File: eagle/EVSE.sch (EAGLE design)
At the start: 21 parts

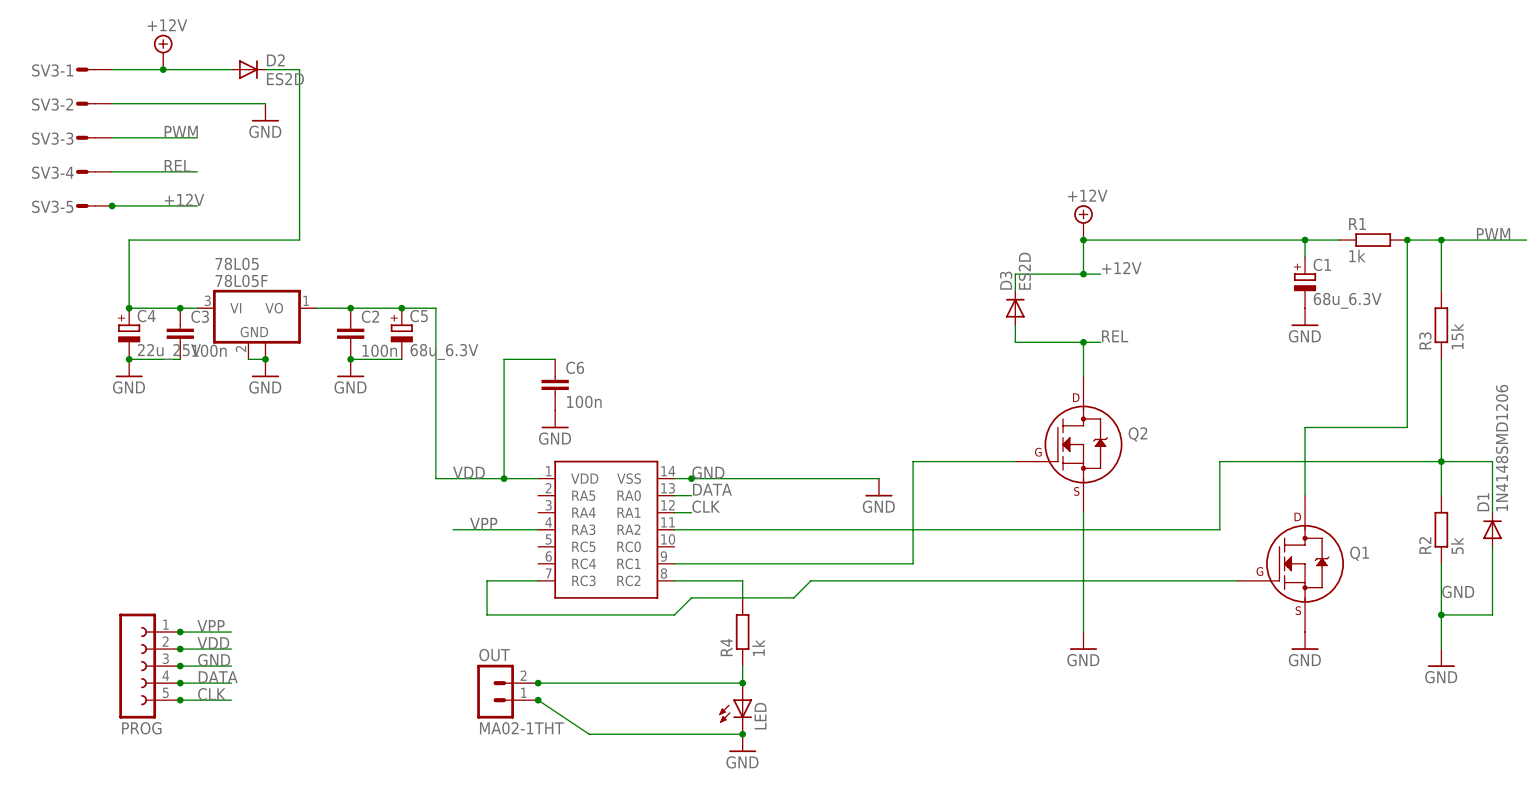
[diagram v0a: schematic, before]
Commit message: Updated board layout - cosmetic changes.
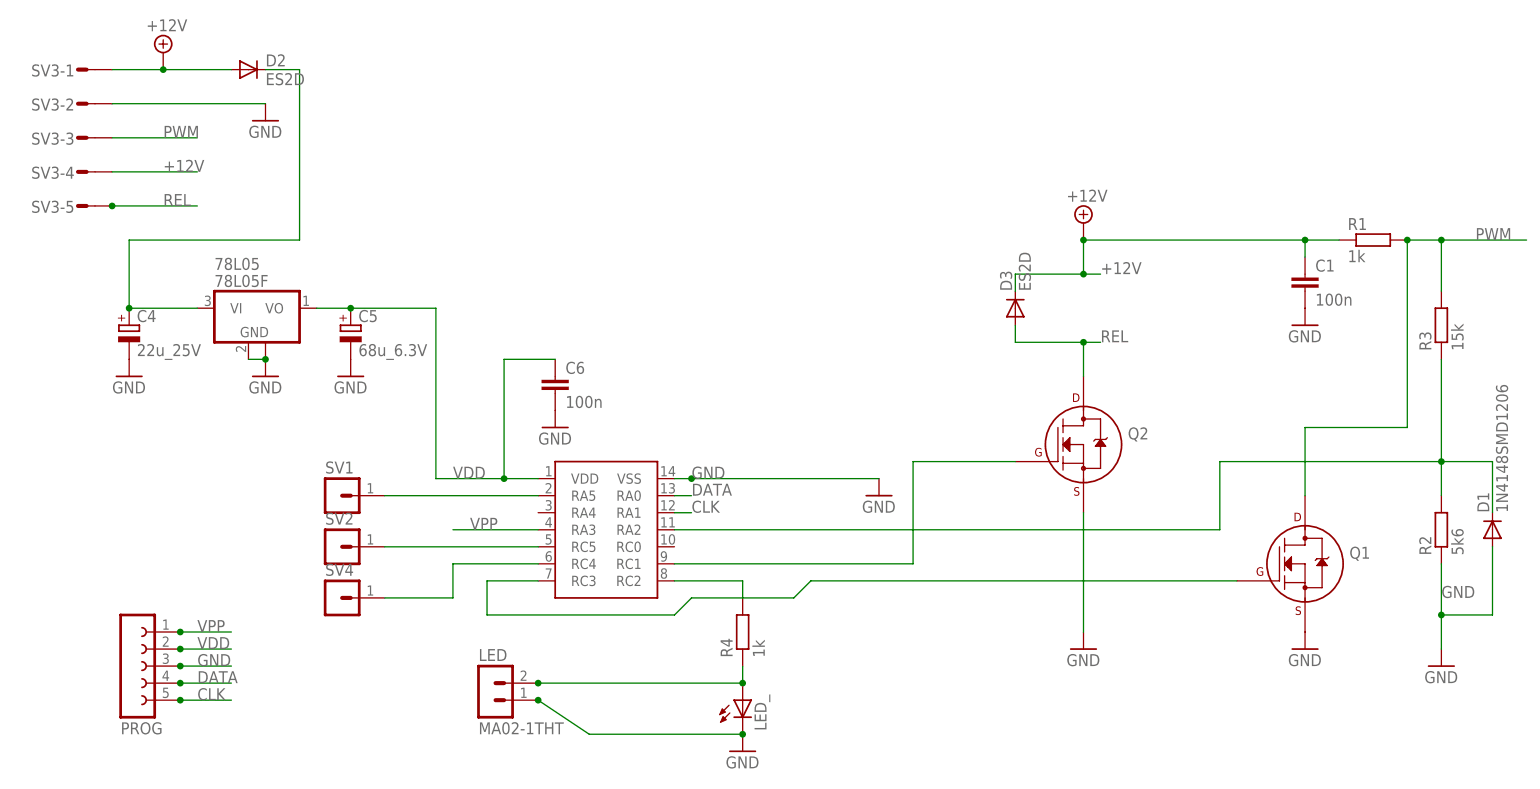
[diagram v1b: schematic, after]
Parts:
- removed C2, C3: 100n, rcl:C-EUC0805
- removed OUT: MA02-1THT, superlibrary:MA02-1THT
- added LED_: (no value), led:LEDSMT1206
- added SV1, SV2, SV4: (no value), superlibrary:PIN-HEADER1
- C1: value 68u_6.3V -> 100n; device rcl:CPOL-EUB/3528-21W -> rcl:C-EUC0805
- LED: value (none) -> MA02-1THT; device led:LEDSMT1206 -> superlibrary:MA02-1THT
- R2: value 5k -> 5k6
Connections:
- new net N$5: PIC16F1825.RA5, SV1.3
- new net N$7: PIC16F1825.RC5, SV2.3
- new net N$8: PIC16F1825.RC4, SV4.3
- net +12V: now also C1.1, SV3-4.S; no longer C1.+, SV3-5.S
- net GND: now also C1.2, LED.1, LED_.C; no longer C1.-, C2.2, C3.2, LED.C, OUT.1
- net N$12: now also LED.2, LED_.A; no longer LED.A, OUT.2
- net N$2: no longer C3.1
- net REL: now also SV3-5.S; no longer SV3-4.S
- net VDD: no longer C2.1
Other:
- moved on the sheet: C5
